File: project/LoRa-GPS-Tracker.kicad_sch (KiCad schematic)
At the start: 45 parts, among them IC1 MCP73831-2-OT, IC103 FT230XS, IC104 NCP705MT30TCG, IC2 MCP100-300D, M1 SIM28ML, M102 RAK3172, Q101 BSS123, Q102 TP0610K, Q103 BSH205G2VL, SW101 ON / OFF, X1 USB_B_Micro, X103 +, X104 -, X3 Conn_Coaxial

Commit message: Version 1
PCB:
- Update build.yaml
- Add PCB variant for KiBot

Signed-off-by: Daniel Kampert <DanielKampert@kampis-elektroecke.de>
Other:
- title: LoRa GPS-Tracker -> LoRa-GPS-Tracker
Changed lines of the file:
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@@
   (paper "A3")
   (title_block
-    (title "LoRa GPS-Tracker")
-    (date "2023-01-01")
+    (title "LoRa-GPS-Tracker")
+    (date "2024-01-07")
     (rev "1.0")
     (company "Kampis-Elektroecke")

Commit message: Version 1.0
Electronics:
- Add jumper for current measurement
- Add jumper to set the RAK module into bootloader mode
- Add capacitor for battery measurement

Testing Firmware:
- Add UART GPS parser
- SubGHz PHY is now using the coordinates from GPS

Firmware:
- Add STM32CubeMX project

Misc:
- Add README

- Add CHANGELOG

Signed-off-by: Daniel Kampert <DanielKampert@kampis-elektroecke.de>
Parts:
- added C103: 100n, Capacitor_SMD:C_0402_1005Metric_Pad0.74x0.62mm_HandSolder, symbol Device:C
- added JP101: PROG, Jumper:SolderJumper-3_P1.3mm_Open_RoundedPad1.0x1.5mm_NumberLabels, symbol Jumper:Jumper_3_Open
- added R114, R115: 0R, Resistor_SMD:R_0402_1005Metric_Pad0.72x0.64mm_HandSolder, symbol Device:R
- R101, R102: value 100R -> 0R; Mfr. Yageo -> Bourns; Mfr. No. RC0402JR-07100RL -> CR0805-J/-000ELF; Order Number 603-RC0402JR-07100RL -> 652-CR0805-J/-000ELF
- R109: Mfr. Yageo -> Bourns; Mfr. No. RC0402JR-070RL -> CR0805-J/-000ELF; Order Number 603-RC0402JR-070RL -> 652-CR0805-J/-000ELF
- R112: value 3k3 -> 0R; footprint Resistor_SMD:R_0402_1005Metric_Pad0.72x0.64mm_HandSolder -> Resistor_SMD:R_0805_2012Metric_Pad1.20x1.40mm_HandSolder; Mfr. Yageo -> Bourns; Mfr. No. RC0402JR-073K3L -> CR0805-J/-000ELF; Order Number 603-RC0402JR-073K3L -> 652-CR0805-J/-000ELF
- renumbered C103 to C104, C104 to C105, C105 to C106, C106 to C107, C107 to C108, C108 to C109, C109 to C110, C110 to C111, C111 to C112, C112 to C113, C113 to C114, R114 to R116, R115 to R117
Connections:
- net +3V0: now also JP101.3 (B)
- net GND: now also C103.2, JP101.1 (A)
- net Rx_GNSS: now also M102.2 (TX2); no longer M102.4 (TX1)
- net Rx_PROG: now also M102.9 (SCL), R115.2; no longer IC103.1 (TXD), M102.1 (RX2)
- net Tx_GNSS: now also M102.1 (RX2); no longer M102.5 (RX1)
- net Tx_PROG: now also M102.10 (SDA), R114.1; no longer IC103.4 (RXD), M102.2 (TX2)
- net V_BAT: now also C103.1
- net at C111.1, IC104.6 (IN), IC2.2 (VDD): now also R112.1; no longer Q103.2 (S), R113.1
- net at R113.2, SW101.1: no longer IC104.4 (EN), R112.2
- net at IC2.1 (~{RST}): now also IC104.4 (EN), R113.1; no longer R112.1
- net at M102.21 (BOOT): now also JP101.2 (C)
- new net: Q103.2 (S), R112.2
- new net: IC103.4 (RXD), R115.1
- new net: IC103.1 (TXD), R114.2
- no-connect marks 32 -> 31
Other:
- moved on the sheet: C104, R113

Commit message: Working on version 1:
Hardware:
- Fix empty ZIP files in KiBot template
- Fix missing drill files in KiBot template
- Add optional SWD connector for debugging
- Add minimal variant without UART console and SWD connector

Nucleo Demo:
- Adding Standby mode and wakeup by UART
- Set internal oscillator frequency to 32 MHz to match the external crystal

Signed-off-by: Daniel Kampert <DanielKampert@kampis-elektroecke.de>
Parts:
- added JP101, JP102: ~, Jumper:SolderJumper-3_P1.3mm_Open_RoundedPad1.0x1.5mm_NumberLabels, symbol Jumper:SolderJumper_3_Open
- added X3: DEBUG, Samtec:SHF-105-01-L-D-SM-TR, symbol Connector:Conn_ARM_JTAG_SWD_10
- C109, C110, IC103, R114, R115: CONFIG (none) -> -MINIMAL
- renumbered JP101 to JP103
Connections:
- net +3V0: now also X3.1 (VTref)
- net GND: now also X3.3 (GND), X3.5 (GND)
- net Rx_PROG: now also JP101.3 (B); no longer R115.2
- net Tx_PROG: now also JP102.3 (B); no longer R114.1
- net Rx_LOG: now reaches M102.4 (TX1)
- net Rx_LOG: now also JP101.1 (A)
- net Tx_LOG: now reaches M102.5 (RX1)
- net Tx_LOG: now also JP102.1 (A)
- net SWDIO: now reaches M102.7 (SWDIO)
- net SWDIO: now also X3.2 (SWDIO/TMS)
- net SWDCLK: now reaches M102.8 (SWCLK)
- net SWDCLK: now also X3.4 (SWDCLK/TCK)
- new net Rx: JP101.2 (C), R115.2
- new net Tx: JP102.2 (C), R114.1
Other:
- note added: "Debug connector"
- note added: "UART bridge"

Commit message: Update build.yml
Add variants to build.yml

Signed-off-by: Daniel Kampert <DanielKampert@kampis-elektroecke.de>
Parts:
- M102: Mfr. (none) -> RAK Wireless; Mfr. No. (none) -> 301025
- X3: CONFIG -MINIMAL -> +DEBUG
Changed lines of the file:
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@@
       (effects (font (size 1.27 1.27)) hide)
     )
-    (property "CONFIG" "-MINIMAL" (at 224.79 254 0)
+    (property "CONFIG" "+DEBUG" (at 224.79 254 0)
       (effects (font (size 1.27 1.27)) hide)
     )
@@
       (effects (font (size 1.27 1.27)) hide)
     )
-    (property "Mfr." "" (at 364.49 72.39 0)
-      (effects (font (size 1.27 1.27)) hide)
-    )
-    (property "Mfr. No." "" (at 364.49 72.39 0)
-      (effects (font (size 1.27 1.27)) hide)
-    )
+    (property "Mfr." "RAK Wireless" (at 364.49 72.39 0)
+      (effects (font (size 1.27 1.27)) hide)
+    )
+    (property "Mfr. No." "301025" (at 364.49 72.39 0)
+      (effects (font (size 1.27 1.27)) hide)
+    )

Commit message: Working on version 1
Hardware:
- Finalize PCB
- Replace expensive components with cheaper ones
- Add GPS antenna
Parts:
- added AE101: GPS Antenna, symbol Device:Antenna
- D101: Mfr. No. SML-P12Y3TT86R -> SML-P12Y2TT86R; Order Number 755-SML-P12Y3TT86R -> 755-SML-P12Y2TT86R
- R103, R104, R111: Mfr. No. RC0402JR-07100KL -> RC0402FR-07100KL; Order Number 603-RC0402JR-07100KL -> 603-RC0402FR-07100KL
- SW101: Mfr. Omron -> CUI Devices; Mfr. No. A6S-1104-PH -> DS04-254-1-01BK-SMT; Order Number 653-A6S1104PH -> 490-DS04254101BK-SMT
- X3: Mfr. No. FTSH-105-01-F-DV-K-P -> FTS-105-01-L-DV-TR; Order Number 200-FTSH10501FDVKPTR -> 200-FTS10501LDVTR
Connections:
- no-connect marks 31 -> 32
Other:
- moved on the sheet: C104, C108, R107

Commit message: Hardware: - Add RESET line for SWD interface - Replace micro USB with USB C
Software:
- Add firmware for LoRa-GPS-Tracker PCB

Signed-off-by: Daniel Kampert <DanielKampert@kampis-elektroecke.de>
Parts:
- removed X1: USB_B_Micro, Wuerth:629105150521, symbol Connector:USB_B_Micro
- added AE102: LoRa Antenna (433 MHz), symbol Device:Antenna
- added R107, R108: 5k1, Resistor_SMD:R_0603_1608Metric, symbol Device:R_Small
- added X101: DEBUG, Connector_USB:USB_C_Receptacle_GCT_USB4105-xx-A_16P_TopMnt_Horizontal, symbol Connector:USB_C_Receptacle_USB2.0
- JP101: value ~ -> RX
- JP102: value ~ -> TX
- JP103: value PROG -> BOOT
- M102: Distributor (none) -> RAK Wireless; Order Number (none) -> 301025
- R101: renamed from R103; now not fitted
- R111: renamed from R107; value 2k -> 10k; Mfr. No. RC0402JR-072KL -> RC0402JR-0710KL; Order Number 603-RC0402JR-072KL -> 603-RC0402JR-0710KL
- renumbered C105 to C104, C104 to C105, C109 to C108, C108 to C109, R101 to R102, R102 to R103, R108 to R109, R109 to R110, R110 to R112, R111 to R113, R112 to R114, R113 to R115, R114 to R116, R115 to R117, R116 to R118, R117 to R119
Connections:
- net +3V0: no longer IC103.11 (~{RESET})
- net GND: now also R107.2, R108.1, X101.A1 (GND), X101.A12 (GND), X101.B1 (GND), X101.B12 (GND), X101.S1 (SHIELD); no longer D101.1 (K)
- net USB_DM: now also X101.A7 (D-), X101.B7 (D-)
- net USB_DP: now also X101.A6 (D+), X101.B6 (D+)
- net V_USB: now also D101.2 (A), X101.A4 (VBUS), X101.A9 (VBUS), X101.B4 (VBUS), X101.B9 (VBUS)
- net at SW101.1: now also IC104.4 (EN), R115.1; no longer R115.2
- net at C108.1, IC103.10 (3V3OUT): now also IC103.11 (~{RESET})
- net at R112.2: now also D101.1 (K); no longer D101.2 (A)
- net ~{RESET}: now reaches X3.10 (~{RESET})
- net ~{RESET}: now also C113.1, M102.22 (~{RST}), R118.2
- new net: IC2.1 (~{RST}), R115.2
- new net: R108.2, X101.B5 (CC2)
- new net: R107.1, X101.A5 (CC1)
- no-connect marks 32 -> 33
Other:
- note added: "NOTE: Charge current is limited to 100 mA."
- moved on the sheet: AE101, C101, C105, C108, C109, C111, C112, D101, IC1, IC104, IC2, Q103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

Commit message: - Upgrade KiBot to support KiCad 8
Signed-off-by: Daniel Kampert <DanielKampert@kampis-elektroecke.de>
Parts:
- removed D101: CHARGE, LED_SMD:LED_0402_1005Metric_Pad0.77x0.64mm_HandSolder, symbol Device:LED
- removed D102: STATUS, LED_SMD:LED_0402_1005Metric_Pad0.77x0.64mm_HandSolder, symbol Device:LED
- removed SW101: ON / OFF, Button_Switch_SMD:SW_DIP_SPSTx01_Slide_Omron_A6S-110x_W8.9mm_P2.54mm, symbol Switch:SW_DIP_x01
- removed X103: +, TestPoint:TestPoint_Pad_2.0x2.0mm, symbol Connector_Generic:Conn_01x01
- removed X104: -, TestPoint:TestPoint_Pad_2.0x2.0mm, symbol Connector_Generic:Conn_01x01
- added D101: SZMM5Z3V3T1G, Diode_SMD:D_SOD-523, symbol Device:D_Zener
- added D103: STATUS, Cree:QLS6B-FKW-CNSNSF043, symbol LED:CLS6B-FKW
- added R120: 120R, Resistor_SMD:R_0402_1005Metric_Pad0.72x0.64mm_HandSolder, symbol Device:R
- added R121: 240R, Resistor_SMD:R_0402_1005Metric_Pad0.72x0.64mm_HandSolder, symbol Device:R
- added SW102: ON/OFF, Button_Switch_SMD:SW_SPDT_PCM12, symbol Switch:SW_DPDT_x2
- added X103: BATTERY, Molex:78171-0002, symbol Connector_Generic:Conn_01x02
- AE102: Mfr. (none) -> DeLOCK; Mfr. No. (none) -> 88915
- IC101: renamed from IC1; symbol Battery_Management:MCP73831-2-OT -> Battery_Management:MCP73832-2-OT; Mfr. No. MCP73831T-2ACI/OT -> MCP73832T-3ACI/OT; Order Number 579-MCP73831T-2ACI/OT -> 579-MCP73832T-3ACI/OT
- R112: value 270R -> 1k; Mfr. No. RC0402JR-07270RL -> RC0402JR-071KL; Order Number 603-RC0402JR-07270RL -> 603-RC0402JR-071KL
- R119: value 270R -> 120R; Mfr. No. RC0402JR-07270RL -> RC0402JR-07120RL; Order Number 603-RC0402JR-07270RL -> 603-RC0402JR-07120RL
- renumbered IC2 to IC102, L1 to L101, M1 to M101, X3 to X102
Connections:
- net BAT: now also X103.1 (Pin_1)
- net GND: now also D101.2 (A), D103.2 (KB), D103.4 (KR), D103.6 (KR), SW102.2 (B), X103.2 (Pin_2)
- net V_USB: now also R112.2
- net at IC104.4 (EN), R115.1: now also SW102.3 (C)
- net CHARGE: now reaches IC101.1 (STAT), R112.1
- net CHARGE: now also M102.29 (PA0), D101.1 (K)
- net at R119.2: now also D103.1 (AB)
- net at R119.1: now also M102.20 (PA9); no longer M102.27 (PB12)
- net at M102.19 (PA8): now also R120.1
- net at M102.6 (PA1): now also R121.1
- new net: D103.3 (AR), R121.2
- new net: D103.5 (AG), R120.2
- no-connect marks 33 -> 31
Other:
- moved on the sheet: C105, C109, C111, C112, C113, C114, IC101, IC102, IC104, JP103, M102, Q103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

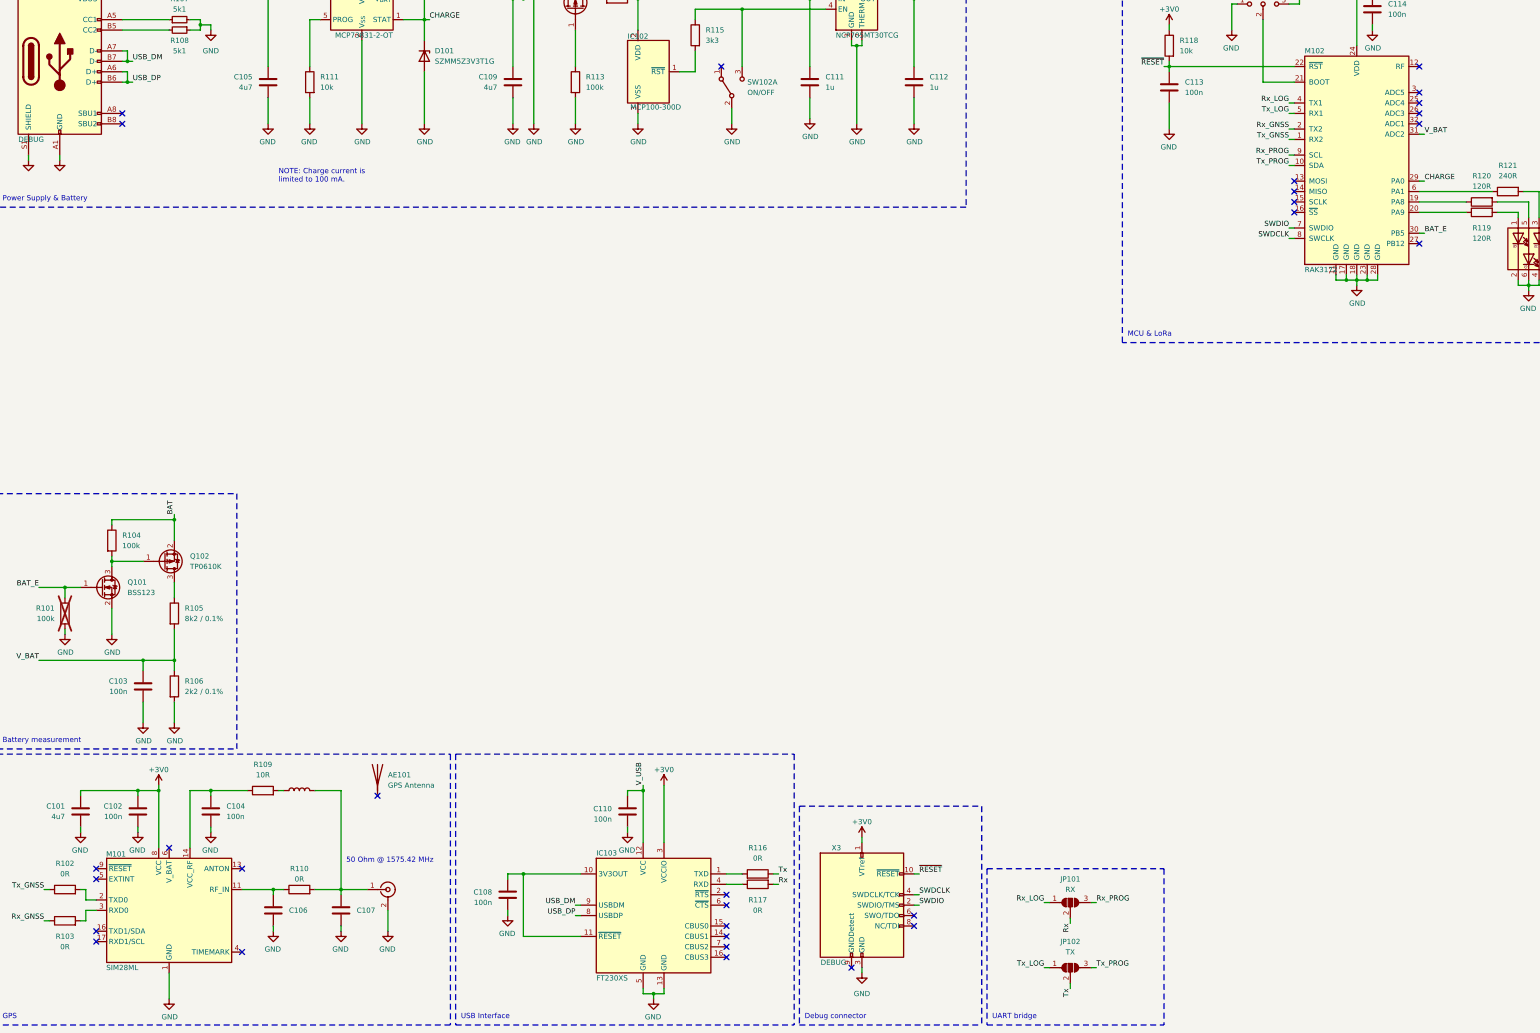
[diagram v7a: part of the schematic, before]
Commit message: - Fix wrong pinout for UART bootloader - Update documentation for bootloader
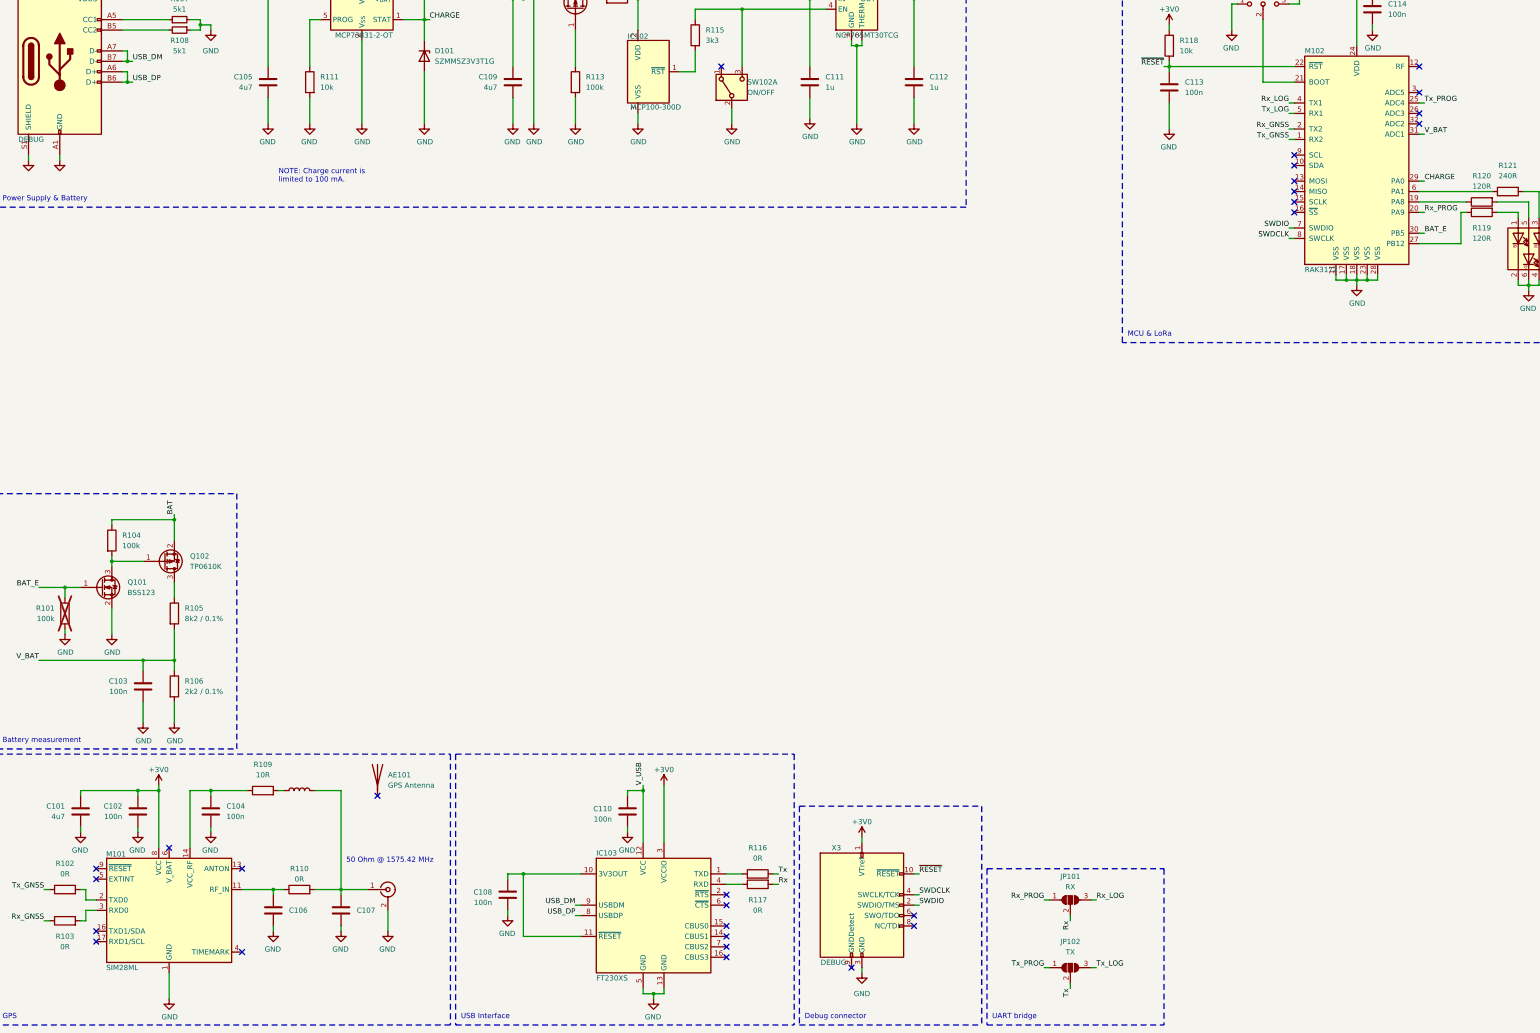
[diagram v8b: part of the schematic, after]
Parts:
- X101: symbol Connector:USB_C_Receptacle_USB2.0 -> Connector:USB_C_Receptacle_USB2.0_14P
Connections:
- net Rx_LOG: now also JP101.3 (B); no longer JP101.1 (A)
- net Rx_PROG: now also JP101.1 (A), M102.20 (PA9); no longer JP101.3 (B), M102.9 (SCL)
- net Tx_LOG: now also JP102.3 (B); no longer JP102.1 (A)
- net Tx_PROG: now also JP102.1 (A), M102.25 (ADC4); no longer JP102.3 (B), M102.10 (SDA)
- net at R119.1: now also M102.27 (PB12); no longer M102.20 (PA9)
- no-connect marks 31 -> 29
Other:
- moved on the sheet: JP101
